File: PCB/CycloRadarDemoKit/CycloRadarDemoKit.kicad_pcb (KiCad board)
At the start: 4 copper layers, 110 x 110 mm, 120 parts, among them J101 I2C conn, J201 ARJM11B1-009-AB-EW2, J501 JTAG, Q101 L8050QLT1G, Q301 L8050QLT1G, Q302 L8050QLT1G, Q401 SI2309CDS, SW101 RESET, SW102 BOOT MODE, U101 ESP32-WROVER-E, U102 RADAR POGO pins, U201 IP101GRI, U301 CP2102N-Axx-xQFN28, U401 INA3221, U402 RT8259, U403 TPS2121RUXR, U404 AP63205WU, U405 AP63203WU, U501 MPU-6050, U502 LSM6DSM, U503 D52MxxM8, Y201 25MHz

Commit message: added more LCSC parts
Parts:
- added C202: 10uF/25V(10%), Capacitor_SMD:C_1206_3216Metric, F.Cu at (148.7, 117.4)
- added C205: 10uF/25V(10%), Capacitor_SMD:C_1206_3216Metric, F.Cu at (148.7, 120.7)
- added C207: 10uF/25V(10%), Capacitor_SMD:C_1206_3216Metric, F.Cu at (148.7, 124.1)
- added C212: 4.7nF/2kV(10%), Capacitor_SMD:C_1206_3216Metric, F.Cu at (148.7, 127.4)
- added C213: 4.7nF/2kV(10%), Capacitor_SMD:C_1206_3216Metric, F.Cu at (148.7, 130.8)
- added C501: 10nF/50V(10%), Capacitor_SMD:C_0603_1608Metric, F.Cu at (159.6, 136.5)
- added C506: 2.2nF/50V(10%), Capacitor_SMD:C_0603_1608Metric, F.Cu at (159.6, 139.0)
- added D301: LED_TX, LED_SMD:LED_0603_1608Metric, F.Cu at (163.6, 117.0)
- added D302: LED_TX, LED_SMD:LED_0603_1608Metric, F.Cu at (163.6, 119.6)
- added D401: LED_12V, LED_SMD:LED_0603_1608Metric, F.Cu at (152.0, 135.7)
- added D403: LED_5V, LED_SMD:LED_0603_1608Metric, F.Cu at (152.0, 138.3)
- added D404: LED_3V3, LED_SMD:LED_0603_1608Metric, F.Cu at (152.0, 140.9)
- added R101: 20K(5%), Resistor_SMD:R_0603_1608Metric, F.Cu at (169.6, 116.9)
- added R102: 10K(1%), Resistor_SMD:R_0603_1608Metric, F.Cu at (169.6, 119.5)
- added R103: 10K(1%), Resistor_SMD:R_0603_1608Metric, F.Cu at (169.6, 122.0)
- added R104: 4.7K, Resistor_SMD:R_0603_1608Metric, F.Cu at (169.6, 124.5)
- added R105: 4.7K, Resistor_SMD:R_0603_1608Metric, F.Cu at (169.6, 127.0)
- added R106: 10K(1%), Resistor_SMD:R_0603_1608Metric, F.Cu at (169.6, 129.5)
- added R109: 1K(1%), Resistor_SMD:R_0603_1608Metric, F.Cu at (169.6, 132.0)
- added R204: 10K(1%), Resistor_SMD:R_0603_1608Metric, F.Cu at (153.6, 116.9)
- added R208: 6.19K(1%), Resistor_SMD:R_0603_1608Metric, F.Cu at (153.6, 119.5)
- added R212: 1M(1%), Resistor_SMD:R_0603_1608Metric, F.Cu at (153.6, 122.0)
- added R301: 1K(1%), Resistor_SMD:R_0603_1608Metric, F.Cu at (159.6, 116.9)
- added R302: 100K(1%), Resistor_SMD:R_0603_1608Metric, F.Cu at (159.6, 119.5)
- added R303: 22.1K(1%), Resistor_SMD:R_0603_1608Metric, F.Cu at (159.6, 122.0)
- added R304: 100K(1%), Resistor_SMD:R_0603_1608Metric, F.Cu at (159.6, 124.5)
- added R305: 47.5K(1%), Resistor_SMD:R_0603_1608Metric, F.Cu at (159.6, 127.0)
- added R306: 100R, Resistor_SMD:R_0603_1608Metric, F.Cu at (159.6, 129.5)
- added R307: 100R, Resistor_SMD:R_0603_1608Metric, F.Cu at (159.6, 132.0)
- added R401: 10K(1%), Resistor_SMD:R_0603_1608Metric, F.Cu at (147.9, 135.7)
- added R410: 2K, Resistor_SMD:R_0603_1608Metric, F.Cu at (147.9, 138.2)
- added R412: 1.1K(1%), Resistor_SMD:R_0603_1608Metric, F.Cu at (147.9, 140.7)
- added R415: 10K(1%), Resistor_SMD:R_0603_1608Metric, F.Cu at (147.9, 143.2)
- added R418: 200R, Resistor_SMD:R_0603_1608Metric, F.Cu at (147.9, 145.7)
- added R419: 2K, Resistor_SMD:R_0603_1608Metric, F.Cu at (147.9, 148.2)
- C503, C504: value 100nF/10V -> 100nF/50V(10%); footprint Capacitor_SMD:C_0603_1608Metric -> Capacitor_SMD:C_0805_2012Metric
- J501: value JTAG -> ANT_JTAG
- R112: value 10K(5%) -> 10K(1%)
- R211: value 270 -> 270R
- R213: value 220 -> 220R
- R402, R403, R404, R405: footprint Resistor_SMD:R_0603_1608Metric -> Capacitor_SMD:C_0603_1608Metric
- moved C505 87.3 mm to (184.0, 132.9)
- moved Q101 87.3 mm to (184.4, 146.1)
- moved R202 87.3 mm to (178.0, 132.5)
- moved R206 87.3 mm to (178.0, 140.0)
- moved R207 87.3 mm to (178.0, 142.5)
- moved L401 87.3 mm to (184.8, 139.0)
- moved R203 87.3 mm to (178.0, 135.0)
- moved R209 87.3 mm to (178.0, 145.0)
- moved R501 87.3 mm to (184.2, 127.7)
- moved C211 87.3 mm to (178.0, 130.0)
- moved C502 87.3 mm to (184.0, 130.4)
- moved R205 87.3 mm to (178.0, 137.5)
- moved U201 74.9 mm to (171.8, 106.8)
- moved J101 51.2 mm to (198.2, 100.9)
- moved R201 51.1 mm to (203.9, 96.5)
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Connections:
- J201 pad 13: (no net) -> unconnected-(J201-NC-Pad13)
- J201 pad 14: (no net) -> unconnected-(J201-NC-Pad14)
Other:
- board text added: "THT connectors are on the back side!!!"
- board text added: "TODO: IP101 clearence problem!!!"
- board text removed: "THT connectors are on back side!!!"

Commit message: PCB ready for review
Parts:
- added R110: LDR, OptoDevice:R_LDR_5.1x4.3mm_P3.4mm_Vertical, F.Cu at (185.6, 52.4)
- added R113: 20K(1%), Resistor_SMD:R_0603_1608Metric, F.Cu at (185.0, 59.2)
- R111: value ??? -> 820R
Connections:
- net /RTS1 renamed /U1RTS
- U101 pad 13: /RXD1 -> /U1TXD
- U101 pad 23: /TXD1 -> /U1TXD
- U503 pad D1: /TXD1 -> /U1TXD
- U503 pad D2: /RXD1 -> /U1RXD

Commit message: PCB after review
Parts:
- removed BZ101: Buzzer, Buzzer_Beeper:Buzzer_D9mm_P5mm
- removed the C301 at (133.8, 99.2)
- removed C303: 0.1uF/50V(10%), Capacitor_SMD:C_0603_1608Metric
- removed C503, C504: 100nF/50V(10%), Capacitor_SMD:C_0805_2012Metric
- removed D304, D305, D306, D307, D308, D309, D310, D311, D312, D313, D314, D315, D316, D317, D318, D319, D320, D321, D322, D323: WS2812B, LED_SMD:LED_SK6812MINI_PLCC4_3.5x3.5mm_P1.75mm
- removed Q101: L8050QLT1G, Package_TO_SOT_SMD:SOT-23
- removed R109: 1K(1%), Resistor_SMD:R_0603_1608Metric
- removed R110: LDR, OptoDevice:R_LDR_5.1x4.3mm_P3.4mm_Vertical
- removed R111: 820R, Resistor_SMD:R_0603_1608Metric
- removed R112: 10K(1%), Resistor_SMD:R_0603_1608Metric
- removed R501: 0R, Resistor_SMD:R_0805_2012Metric
- removed the R502 at (104.5, 99.6)
- removed U502: LSM6DSM, Package_LGA:LGA-14_3x2.5mm_P0.5mm_LayoutBorder3x4y
- added BZ601: Buzzer, Buzzer_Beeper:Buzzer_D9mm_P5mm, F.Cu at (54.7, 148.1)
- added C105: 100nF/50V(10%), Capacitor_SMD:C_0603_1608Metric, F.Cu at (197.6, 112.1)
- added C507: 100nF/50V(10%), Capacitor_SMD:C_0603_1608Metric, F.Cu at (197.2, 120.0)
- added D601: B5819W, Diode_SMD:D_SOD-123, F.Cu at (69.2, 150.4)
- added D602: WS2812B, LED_SMD:LED_SK6812MINI_PLCC4_3.5x3.5mm_P1.75mm, F.Cu at (55.6, 120.3)
- added D603: WS2812B, LED_SMD:LED_SK6812MINI_PLCC4_3.5x3.5mm_P1.75mm, F.Cu at (55.6, 125.3)
- added D604: WS2812B, LED_SMD:LED_SK6812MINI_PLCC4_3.5x3.5mm_P1.75mm, F.Cu at (55.6, 130.4)
- added D605: WS2812B, LED_SMD:LED_SK6812MINI_PLCC4_3.5x3.5mm_P1.75mm, F.Cu at (55.6, 135.4)
- added D606: WS2812B, LED_SMD:LED_SK6812MINI_PLCC4_3.5x3.5mm_P1.75mm, F.Cu at (55.6, 140.5)
- added D607: WS2812B, LED_SMD:LED_SK6812MINI_PLCC4_3.5x3.5mm_P1.75mm, F.Cu at (62.6, 120.3)
- added D608: WS2812B, LED_SMD:LED_SK6812MINI_PLCC4_3.5x3.5mm_P1.75mm, F.Cu at (62.6, 125.3)
- added D609: WS2812B, LED_SMD:LED_SK6812MINI_PLCC4_3.5x3.5mm_P1.75mm, F.Cu at (62.6, 130.4)
- added D610: WS2812B, LED_SMD:LED_SK6812MINI_PLCC4_3.5x3.5mm_P1.75mm, F.Cu at (62.6, 135.4)
- added D611: WS2812B, LED_SMD:LED_SK6812MINI_PLCC4_3.5x3.5mm_P1.75mm, F.Cu at (62.6, 140.5)
- added D612: WS2812B, LED_SMD:LED_SK6812MINI_PLCC4_3.5x3.5mm_P1.75mm, F.Cu at (69.6, 120.3)
- added D613: WS2812B, LED_SMD:LED_SK6812MINI_PLCC4_3.5x3.5mm_P1.75mm, F.Cu at (69.6, 125.3)
- added D614: WS2812B, LED_SMD:LED_SK6812MINI_PLCC4_3.5x3.5mm_P1.75mm, F.Cu at (69.6, 130.4)
- added D615: WS2812B, LED_SMD:LED_SK6812MINI_PLCC4_3.5x3.5mm_P1.75mm, F.Cu at (69.6, 135.4)
- added D616: WS2812B, LED_SMD:LED_SK6812MINI_PLCC4_3.5x3.5mm_P1.75mm, F.Cu at (69.6, 140.5)
- added D617: WS2812B, LED_SMD:LED_SK6812MINI_PLCC4_3.5x3.5mm_P1.75mm, F.Cu at (76.6, 120.3)
- added D618: WS2812B, LED_SMD:LED_SK6812MINI_PLCC4_3.5x3.5mm_P1.75mm, F.Cu at (76.6, 125.3)
- added D619: WS2812B, LED_SMD:LED_SK6812MINI_PLCC4_3.5x3.5mm_P1.75mm, F.Cu at (76.6, 130.4)
- added D620: WS2812B, LED_SMD:LED_SK6812MINI_PLCC4_3.5x3.5mm_P1.75mm, F.Cu at (76.6, 135.4)
- added D621: WS2812B, LED_SMD:LED_SK6812MINI_PLCC4_3.5x3.5mm_P1.75mm, F.Cu at (76.6, 140.5)
- added FB301: YI160808Z101-3R0T, Resistor_SMD:R_0603_1608Metric, F.Cu at (110.4, 86.8)
- added FB501: YI160808Z101-3R0T, Resistor_SMD:R_0603_1608Metric, F.Cu at (114.7, 101.5)
- added J104: Radar debug, Connector_FFC-FPC:AFC30-S10FCC-00, F.Cu at (112.2, 125.5)
- added J301: USB_C_Receptacle_USB2.0, Connector_USB:USB_C_Receptacle_GCT_USB4110, F.Cu at (221.6, 59.2)
- added Q601: L8050QLT1G, Package_TO_SOT_SMD:SOT-23, F.Cu at (75.5, 145.2)
- added R114: 10K(1%), Resistor_SMD:R_0603_1608Metric, F.Cu at (84.2, 125.7)
- added R413: 0R, Resistor_SMD:R_0805_2012Metric, F.Cu at (191.4, 112.3)
- added R415: NC, Resistor_SMD:R_0805_2012Metric, F.Cu at (191.4, 115.3)
- added R504: 10K(1%), Resistor_SMD:R_0603_1608Metric, F.Cu at (197.2, 122.5)
- added R601: LDR, OptoDevice:R_LDR_5.1x4.3mm_P3.4mm_Vertical, F.Cu at (68.0, 145.9)
- added R602: 20K(1%), Resistor_SMD:R_0603_1608Metric, F.Cu at (64.3, 144.2)
- added R603: 10K(1%), Resistor_SMD:R_0603_1608Metric, F.Cu at (64.3, 146.8)
- added R604: 820R, Resistor_SMD:R_0603_1608Metric, F.Cu at (64.3, 149.3)
- added TP201: TXER, TestPoint:TestPoint_Pad_D2.0mm, F.Cu at (105.7, 51.1)
- added TP202: RESET, TestPoint:TestPoint_Pad_D2.0mm, F.Cu at (105.7, 56.2)
- added TP203: RXER, TestPoint:TestPoint_Pad_D2.0mm, F.Cu at (105.7, 61.2)
- added TP501: SLEEP, TestPoint:TestPoint_Pad_D2.0mm, F.Cu at (112.8, 51.1)
- added TP502: ~{SUSPEND}, TestPoint:TestPoint_Pad_D2.0mm, F.Cu at (112.8, 56.2)
- added TP503: GPIO, TestPoint:TestPoint_Pad_D2.0mm, F.Cu at (112.8, 61.2)
- C102: value 1uF/50V(10%) -> 10uF
- C104, C201, C210, C211, C502, C505: value 0.1uF/50V(10%) -> 100nF/50V(10%)
- C203, C204, C206: value 0.1uF/50V(10%) -> 1uF/50V(10%)
- C401: renamed from C411; footprint Capacitor_SMD:C_0805_2012Metric -> Capacitor_SMD:C_0603_1608Metric
- C410: renamed from C408; footprint Capacitor_SMD:C_0805_2012Metric -> Capacitor_SMD:C_0603_1608Metric
- C411: renamed from C406; footprint Capacitor_SMD:C_0805_2012Metric -> Capacitor_SMD:C_0603_1608Metric
- C501: footprint Capacitor_SMD:C_0603_1608Metric -> Capacitor_SMD:C_0402_1005Metric
- J101: footprint Connector_PinHeader_1.27mm:PinHeader_1x05_P1.27mm_Vertical -> Connector_PinHeader_1.27mm:PinHeader_1x06_P1.27mm_Vertical
- JP501, JP502, JP503: footprint Jumper:SolderJumper-3_P1.3mm_Open_RoundedPad1.0x1.5mm_NumberLabels -> Jumper:SolderJumper-3_P1.3mm_Bridged12_RoundedPad1.0x1.5mm_NumberLabels
- R113: value 20K(1%) -> 1K(1%)
- moved C203 72.8 mm to (191.2, 120.0)
- moved C204 72.8 mm to (191.2, 122.5)
- moved U102 58.3 mm to (275.8, 99.0), turned to 180 degrees
- moved R113 56.8 mm to (197.6, 114.6)
- moved JP502 7.24 mm to (115.5, 94.9)
- moved JP503 7.24 mm to (115.5, 98.5)
- renumbered C304 to C301, C412 to C402, C413 to C403, C414 to C404, C401 to C405, C402 to C406, C403 to C407, C404 to C408, C405 to C409, C407 to C412, C409 to C413, C410 to C414, D101 to D102, D102 to D103, D404 to D401, D401 to D402, D402 to D403, D405 to D404, D403 to D405, L403 to L401, L401 to L402, L402 to L403, R417 to R402, R418 to R403, R402 to R404, R403 to R405, R404 to R406, R405 to R407, R406 to R408, R407 to R409, R408 to R410, R409 to R411, R410 to R412, R411 to R414, R412 to R416, R414 to R417, R415 to R418, R413 to R419, R419 to R420, R503 to R502, R504 to R503, U405 to U401, U401 to U402, U402 to U403, U403 to U404, U404 to U405
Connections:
- net /USB + LED/DTR renamed /USB/DTR
- net /USB + LED/RTS renamed /USB/RTS
- net /USB + LED/RXD renamed /USB/RXD
- net /USB + LED/TXD renamed /USB/TXD
- C102 pad 1: Net-(U101-3V3) -> +3V3
- D405 pad 2: Net-(D403-A) -> Net-(D405-A)
- J101 pad 1: SDA -> /IMU_INT
- J101 pad 2: SCL -> SDA
- J101 pad 3: +3V3 -> SCL
- J101 pad 4: GND -> +3V3
- J101 pad 5: /Radar_GPIO -> GND
- J501 pad 10: /EN -> /IMU + ANT/~{RST}
- JP501 pad 1: /IMU + ANT/VCC -> GND
- JP501 pad 3: GND -> /IMU + ANT/VCC
- JP503 pad 1: /IMU + ANT/VCC -> GND
- JP503 pad 3: GND -> /IMU + ANT/VCC
- R113 pad 1: /Photo_res -> Net-(C105-Pad1)
- R113 pad 2: +3V3 -> /IO0_TACT
- R419 pad 2: Net-(D403-A) -> Net-(D405-A)
- SW102 pad 1: Net-(R109-Pad1) -> GND
- SW102 pad 2: /IO0_TACT -> Net-(C105-Pad1)
- U101 pad 2: Net-(U101-3V3) -> +3V3
- U101 pad 26: /LED_DIN -> /LED
- U404 pad 6: Net-(D403-A) -> Net-(U404-PR1)
- U404 pad 7: Net-(D403-A) -> Net-(D405-A)
- U503 pad E6: /EN -> /IMU + ANT/~{RST}
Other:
- board text added: "TODO: Consider 0402!!!"
- board text added: "TODO: Double side assembly!!!"
- board text added: "TODO: Length matching on RMII"
- board text added: "TOP"

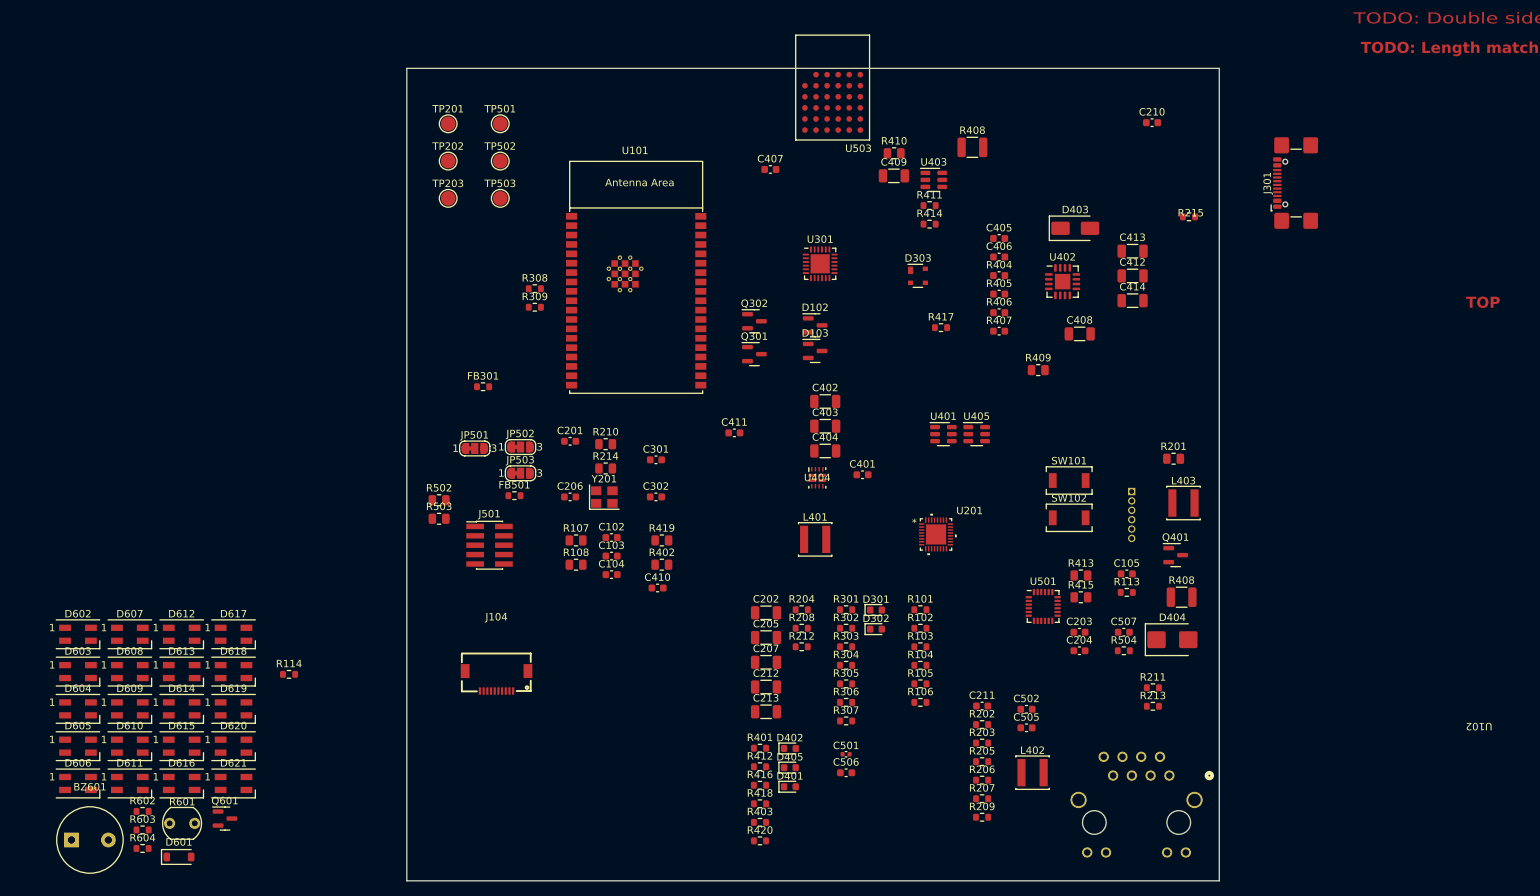
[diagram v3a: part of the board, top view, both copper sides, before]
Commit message: Schematic edited, split sheets
improved PM diagram
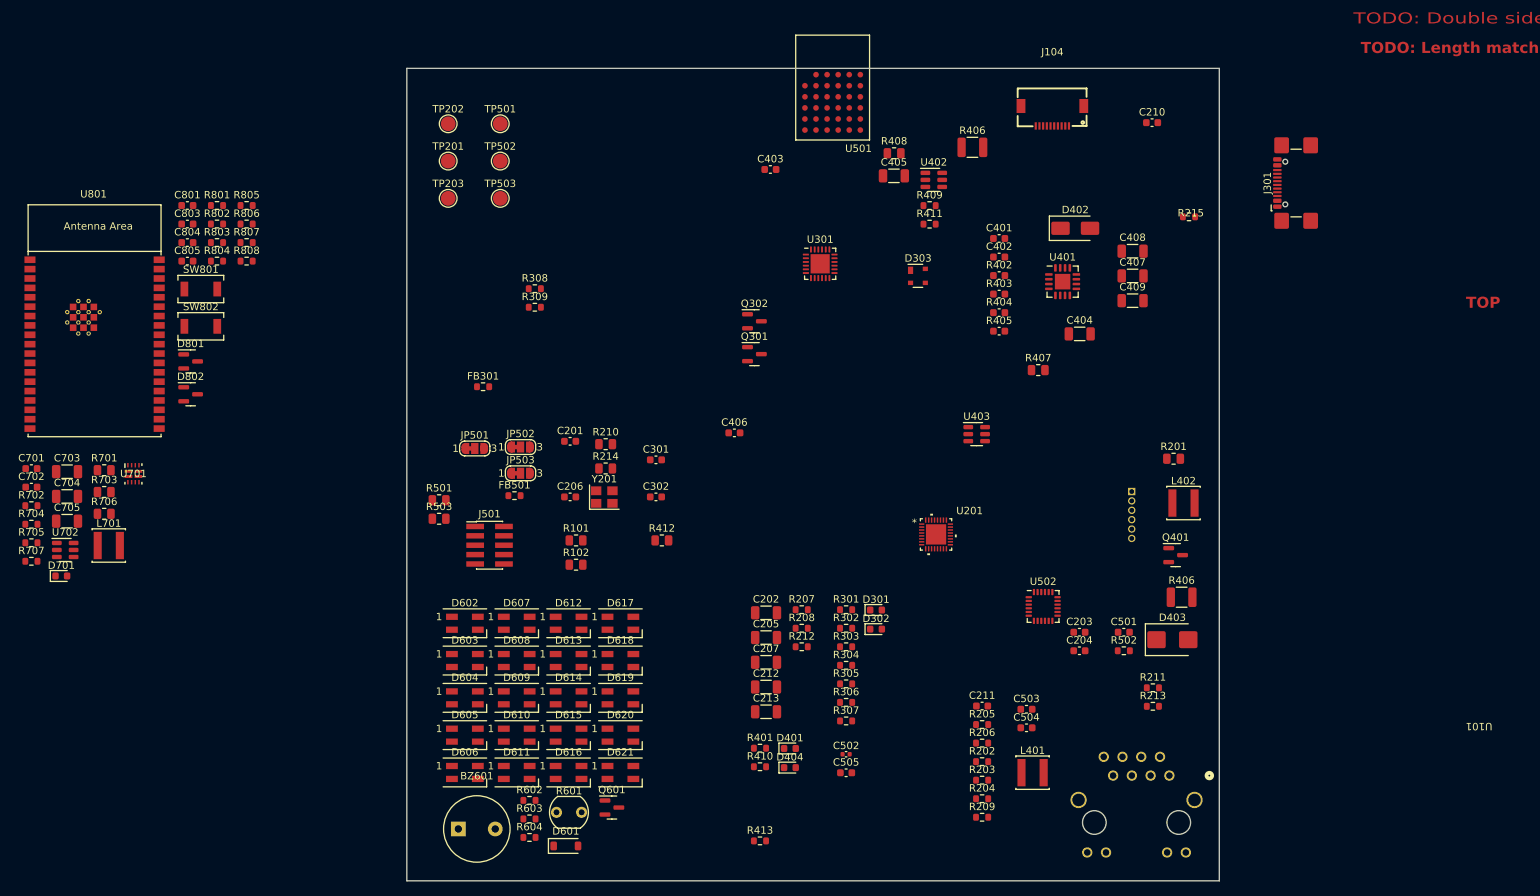
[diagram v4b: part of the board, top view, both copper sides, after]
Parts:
- removed C102: 10uF, Capacitor_SMD:C_0603_1608Metric
- removed C103: 1uF/50V(10%), Capacitor_SMD:C_0603_1608Metric
- removed C104, C105, C410: 100nF/50V(10%), Capacitor_SMD:C_0603_1608Metric
- removed the C401 at (161.8, 98.7)
- removed the C402 at (156.8, 88.8)
- removed the C403 at (156.8, 92.1)
- removed the C404 at (156.8, 95.5)
- removed D102, D103: BAT54A, Package_TO_SOT_SMD:SOT-23
- removed the D401 at (152.0, 140.9)
- removed the L401 at (155.4, 107.4)
- removed the R101 at (169.6, 116.9)
- removed the R102 at (169.6, 119.5)
- removed R103, R106, R114, R418: 10K(1%), Resistor_SMD:R_0603_1608Metric
- removed R104, R105: 4.7K, Resistor_SMD:R_0603_1608Metric
- removed R113: 1K(1%), Resistor_SMD:R_0603_1608Metric
- removed the R402 at (134.6, 110.8)
- removed the R403 at (147.9, 145.7)
- removed the R413 at (191.4, 112.3)
- removed R415: NC, Resistor_SMD:R_0805_2012Metric
- removed R416: 1.1K(1%), Resistor_SMD:R_0603_1608Metric
- removed R417: 47k(1%), Resistor_SMD:R_0603_1608Metric
- removed SW101: RESET, Button_Switch_SMD:SW_SPST_TS-1088R
- removed SW102: BOOT MODE, Button_Switch_SMD:SW_SPST_TS-1088R
- removed the U101 at (131.2, 71.9)
- removed the U401 at (172.8, 93.2)
- removed U404: TPS2121RUXR, TPS2121:TPS2121
- added C701: 100nF/50V(10%), Capacitor_SMD:C_0603_1608Metric, F.Cu at (49.3, 97.8)
- added C702: 100nF/50V(10%), Capacitor_SMD:C_0603_1608Metric, F.Cu at (49.3, 100.3)
- added C703: 22uF/16V(20%), Capacitor_SMD:C_1206_3216Metric, F.Cu at (54.1, 98.3)
- added C704: 10uF/25V(10%), Capacitor_SMD:C_1206_3216Metric, F.Cu at (54.1, 101.6)
- added C705: 22uF/16V(20%), Capacitor_SMD:C_1206_3216Metric, F.Cu at (54.1, 105.0)
- added C801: 10uF, Capacitor_SMD:C_0603_1608Metric, F.Cu at (70.4, 62.2)
- added C803: 1uF/50V(10%), Capacitor_SMD:C_0603_1608Metric, F.Cu at (70.4, 64.7)
- added C804: 100nF/50V(10%), Capacitor_SMD:C_0603_1608Metric, F.Cu at (70.4, 67.2)
- added C805: 100nF/50V(10%), Capacitor_SMD:C_0603_1608Metric, F.Cu at (70.4, 69.7)
- added D701: LED_3V3, LED_SMD:LED_0603_1608Metric, F.Cu at (53.3, 112.4)
- added D801: BAT54A, Package_TO_SOT_SMD:SOT-23, F.Cu at (70.8, 83.3)
- added D802: BAT54A, Package_TO_SOT_SMD:SOT-23, F.Cu at (70.8, 87.8)
- added L701: 4.7uH/2.85A, Inductor_SMD:L_Sunlord_SWPA4020S, F.Cu at (59.8, 108.2)
- added R701: 0R, Resistor_SMD:R_0805_2012Metric, F.Cu at (59.1, 98.1)
- added R702: 1.1K(1%), Resistor_SMD:R_0603_1608Metric, F.Cu at (49.3, 102.9)
- added R703: NC, Resistor_SMD:R_0805_2012Metric, F.Cu at (59.1, 101.0)
- added R704: 47k(1%), Resistor_SMD:R_0603_1608Metric, F.Cu at (49.3, 105.4)
- added R705: 10K(1%), Resistor_SMD:R_0603_1608Metric, F.Cu at (49.3, 107.9)
- added R706: 0R, Resistor_SMD:R_0805_2012Metric, F.Cu at (59.1, 104.0)
- added R707: 200R, Resistor_SMD:R_0603_1608Metric, F.Cu at (49.3, 110.4)
- added R801: 20K(5%), Resistor_SMD:R_0603_1608Metric, F.Cu at (74.4, 62.2)
- added R802: 10K(1%), Resistor_SMD:R_0603_1608Metric, F.Cu at (74.4, 64.7)
- added R803: 10K(1%), Resistor_SMD:R_0603_1608Metric, F.Cu at (74.4, 67.2)
- added R804: 10K(1%), Resistor_SMD:R_0603_1608Metric, F.Cu at (74.4, 69.7)
- added R805: 4.7K, Resistor_SMD:R_0603_1608Metric, F.Cu at (78.4, 62.2)
- added R806: 4.7K, Resistor_SMD:R_0603_1608Metric, F.Cu at (78.4, 64.7)
- added R807: 10K(1%), Resistor_SMD:R_0603_1608Metric, F.Cu at (78.4, 67.2)
- added R808: 1K(1%), Resistor_SMD:R_0603_1608Metric, F.Cu at (78.4, 69.7)
- added SW801: RESET, Button_Switch_SMD:SW_SPST_TS-1088R, F.Cu at (72.2, 73.5)
- added SW802: BOOT MODE, Button_Switch_SMD:SW_SPST_TS-1088R, F.Cu at (72.2, 78.6)
- added U701: TPS2121RUXR, TPS2121:TPS2121, F.Cu at (63.1, 98.5)
- added U702: AP63203WU, Package_TO_SOT_SMD:TSOT-23-6, F.Cu at (53.9, 108.9)
- added U801: ESP32-WROVER-E-N16R8, Espressif:ESP32-WROVER-E_ThermalVias, F.Cu at (57.8, 77.8)
- U301: value CP2102N-Axx-xQFN28 -> CP2102N-Axx-xQFN24
- moved J104 107.3 mm to (187.5, 49.0)
- moved D617 52.4 mm to (129.0, 118.8)
- moved D618 52.4 mm to (129.0, 123.8)
- moved D619 52.4 mm to (129.0, 128.9)
- moved D620 52.4 mm to (129.0, 133.9)
- moved D621 52.4 mm to (129.0, 139.0)
- moved BZ601 52.4 mm to (107.1, 146.6)
- moved D607 52.4 mm to (115.0, 118.8)
- moved D608 52.4 mm to (115.0, 123.8)
- moved D609 52.4 mm to (115.0, 128.9)
- moved D610 52.4 mm to (115.0, 133.9)
- moved D611 52.4 mm to (115.0, 139.0)
- moved D601 52.4 mm to (121.6, 148.9)
- moved D602 52.4 mm to (108.0, 118.8)
- moved D603 52.4 mm to (108.0, 123.8)
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- renumbered C405 to C401, C406 to C402, C407 to C403, C408 to C404, C409 to C405, C411 to C406, C412 to C407, C413 to C408, C414 to C409, C507 to C501, C501 to C502, C502 to C503, C505 to C504, C506 to C505, D402 to D401, D403 to D402, D404 to D403, D405 to D404, L402 to L401, L403 to L402, R107 to R101, R108 to R102, R205 to R202, R206 to R203, R207 to R204, R202 to R205, R203 to R206, R204 to R207, R404 to R402, R405 to R403, R406 to R404, R407 to R405, R408 to R406, R409 to R407, R410 to R408, R411 to R409, R412 to R410, R414 to R411, R419 to R412, R420 to R413, R502 to R501, R504 to R502, TP202 to TP201, TP201 to TP202, U102 to U101, U402 to U401, U403 to U402, U405 to U403, U503 to U501, U501 to U502
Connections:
- net /MAC_CLK renamed /PHY_CLK
- net /PMIC_INT renamed /ESP32/PMIC_INT
- net /Photo_res renamed /ESP32/Photo_res
- net Net-(D405-A) renamed /20V + 12V/Battery 5V
- net VBUS renamed /5V + 3V3/USB 5V
- D602 pad 4: /LED -> /ESP32/LED
- Q301 pad 3: /IO0_AUTO -> /ESP32/IO0_AUTO
- Q302 pad 3: /EN_AUTO -> /ESP32/EN_AUTO
- R603 pad 2: /Buzzer -> /ESP32/Buzzer
- U402 pad 4: /12V_DIS -> /ESP32/12V_DIS
- U501 pad D1: /U1TXD -> /ESP32/U1TXD
- U501 pad D2: /U1RXD -> /ESP32/U1RXD
- U501 pad F2: /U1RTS -> /ESP32/U1RTS

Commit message: starting the mockup
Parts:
- added J102: CAN, Connector_Molex:Molex_39501-1003, B.Cu at (146.5, 133.2)
- added J103: 100BASE-T1, Connector_Molex:Molex_KK-254_AE-6410-04A_1x04_P2.54mm_Vertical, B.Cu at (154.4, 140.2)
- added J401: 20-16V Supply Voltage, Connector_Molex:Molex_39521-1002, B.Cu at (134.8, 140.0)
- added R103: 120, Resistor_SMD:R_0603_1608Metric, F.Cu at (88.2, 147.2)
- BZ601, J104, R601: moved to B.Cu
- J201: footprint Connector_RJ:RJ45_Abracon_ARJM11B1-009-AB-EW2_ABR -> Connector_RJ:CONN_JXD2-0Z10NL_PUL
- U101: footprint alps_modules:ALPS Generic Radar 5 -> alps_modules:ALPS_USRR5
- moved C211 153.9 mm to (57.6, 225.8)
- moved C501 153.9 mm to (76.8, 215.8)
- moved D401 153.9 mm to (31.6, 231.6)
- moved Q401 153.9 mm to (83.8, 205.4)
- moved R202 153.9 mm to (57.6, 233.4)
- moved C203 153.9 mm to (70.8, 215.8)
- moved C204 153.9 mm to (70.8, 218.3)
- moved C401 153.9 mm to (59.9, 162.5)
- moved C402 153.9 mm to (59.9, 165.0)
- moved C404 153.9 mm to (70.8, 175.4)
- moved C407 153.9 mm to (78.0, 167.6)
- moved C408 153.9 mm to (78.0, 164.2)
- moved C409 153.9 mm to (78.0, 170.9)
- moved C502 153.9 mm to (39.2, 232.4)
- moved C503 153.9 mm to (63.6, 226.3)
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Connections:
- J201 pad 13: unconnected-(J201-NC-Pad13) -> (no net)
- J201 pad 14: unconnected-(J201-NC-Pad14) -> (no net)
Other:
- board size 110 x 110 mm -> 58.8 x 117.8 mm
- board text removed: "TOP"
